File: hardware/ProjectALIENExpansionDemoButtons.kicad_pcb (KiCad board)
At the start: 2 copper layers, 69.1 x 19.8 mm, 8 parts, among them J1 Excess GPIO Pins, J2 Voltage Breakout

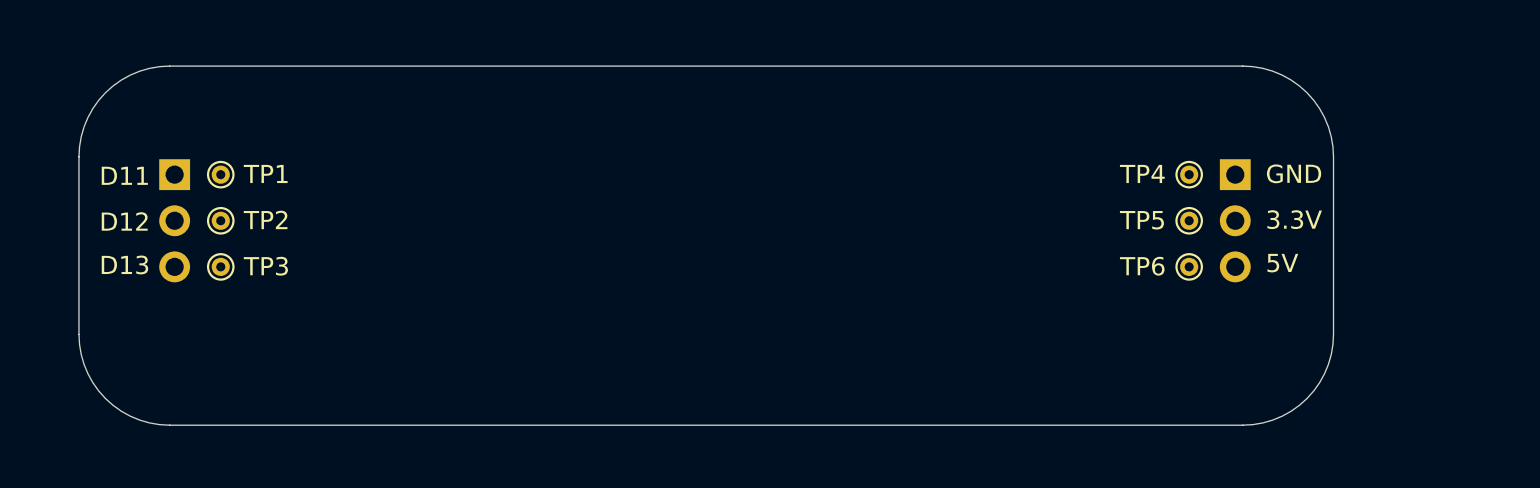
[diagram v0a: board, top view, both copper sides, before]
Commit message: Wired up buttons
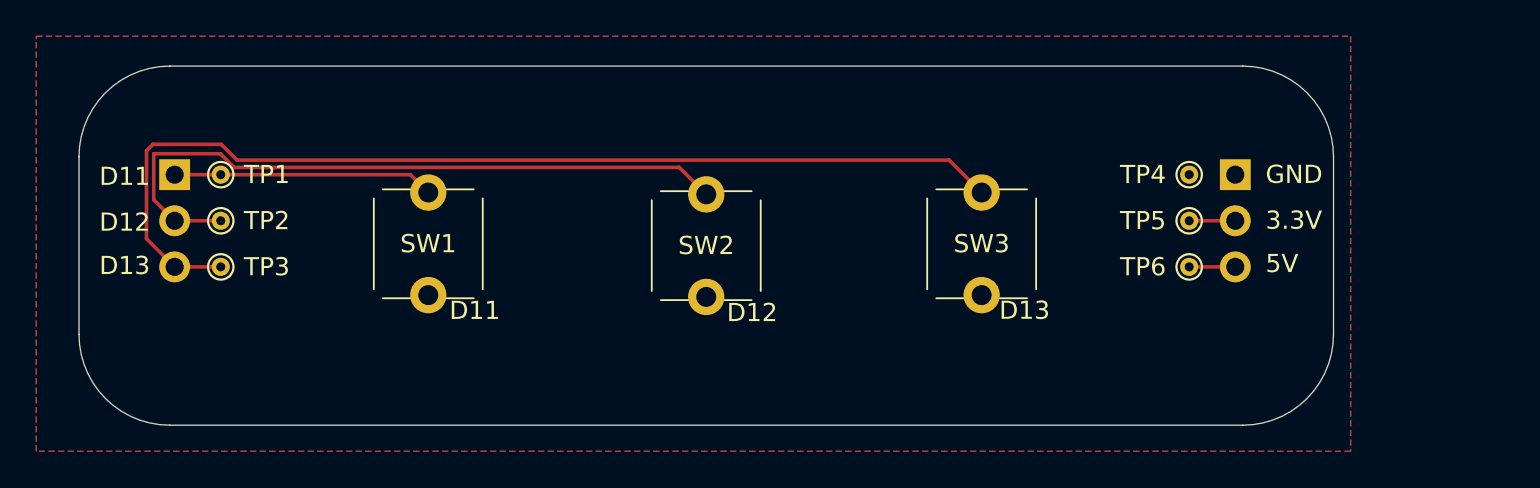
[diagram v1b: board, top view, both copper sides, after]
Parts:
- added SW1: Demo 1, Two_Pin_Through_Hole_Push_Button:Two_Pin_Through_Hole_Push_Button, F.Cu at (123.2, 129.5)
- added SW2: Demo 2, Two_Pin_Through_Hole_Push_Button:Two_Pin_Through_Hole_Push_Button, F.Cu at (138.5, 129.6)
- added SW3: Demo 3, Two_Pin_Through_Hole_Push_Button:Two_Pin_Through_Hole_Push_Button, F.Cu at (153.7, 129.5)
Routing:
- net D13: track 0.00 -> 56.8 mm
- net D12: track 0.00 -> 38.1 mm
- net D11: track 0.00 -> 14.4 mm
- net +5V: track 0.00 -> 2.54 mm
- net +3.3V: track 0.00 -> 2.54 mm
- added copper zone on B.Cu, net GND
- added copper zone on F.Cu, net GND

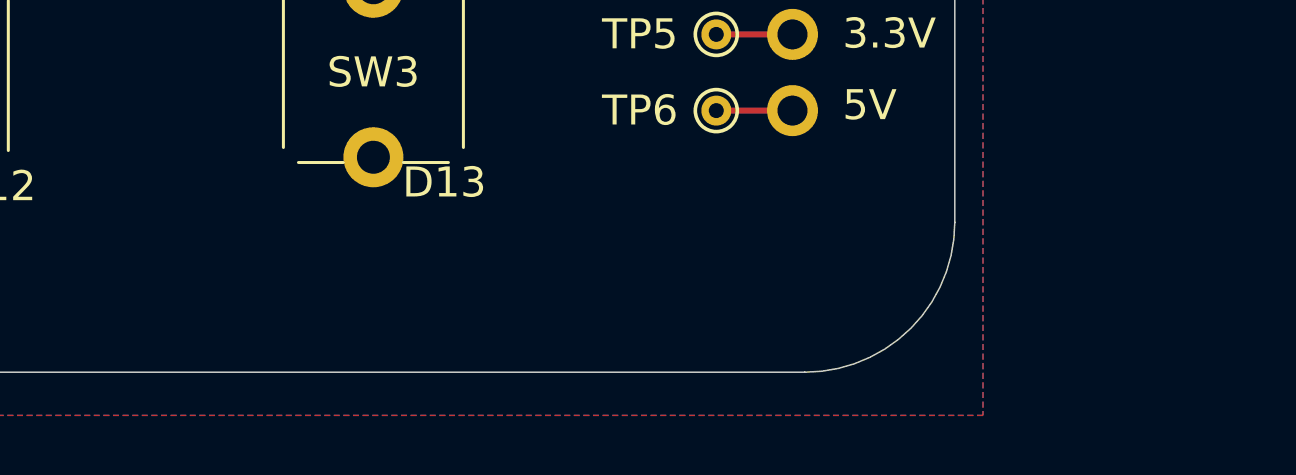
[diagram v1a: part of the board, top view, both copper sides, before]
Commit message: Added title to silkscreen
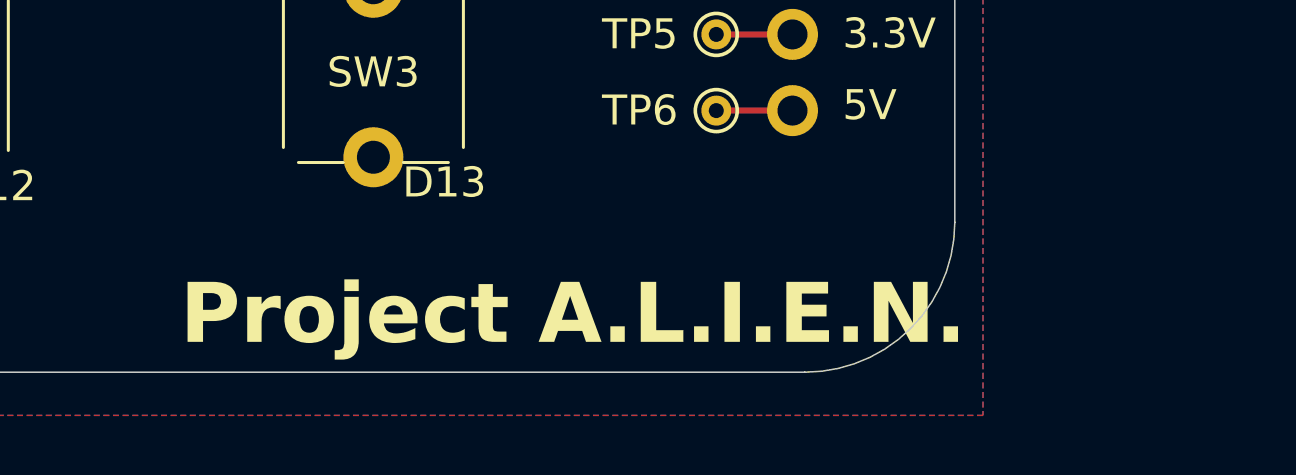
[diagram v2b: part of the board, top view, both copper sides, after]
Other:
- board text added: "Project A.L.I.E.N."
- board text added: "github.com/HBoyd255/project-alien"
